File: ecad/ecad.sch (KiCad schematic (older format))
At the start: 27 parts, among them J1 Conn_01x03_Female, J10 Conn_01x05_Female, J4 Conn_01x03_Female, J5 Conn_01x03_Female, J6 Conn_01x03_Female, J7 Conn_01x05_Female, J8 Conn_01x05_Female, J9 Conn_01x05_Female, U1 DHT11, U2 ABX00012

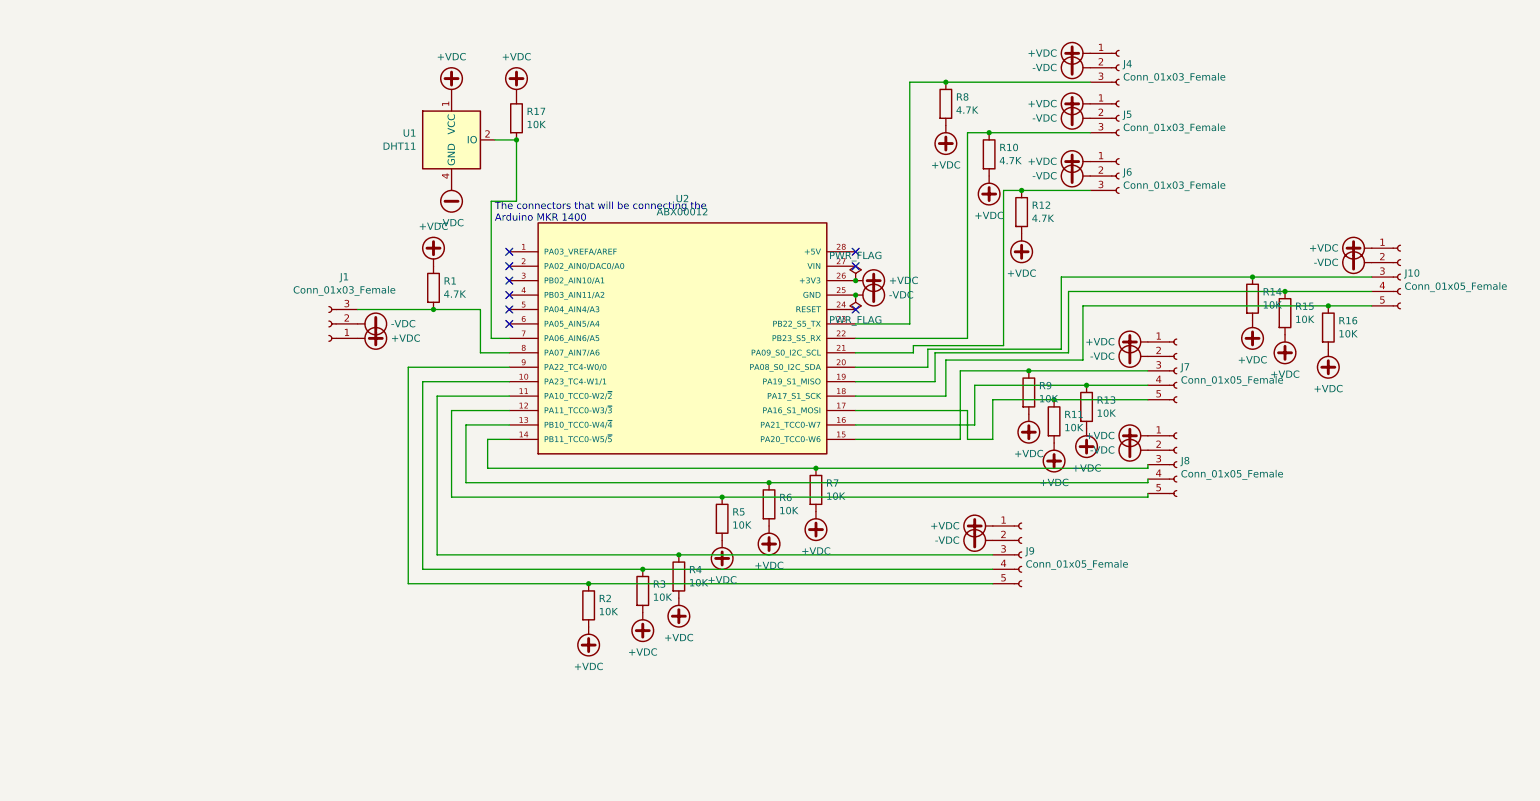
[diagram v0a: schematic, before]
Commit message: add more comments to the schematic
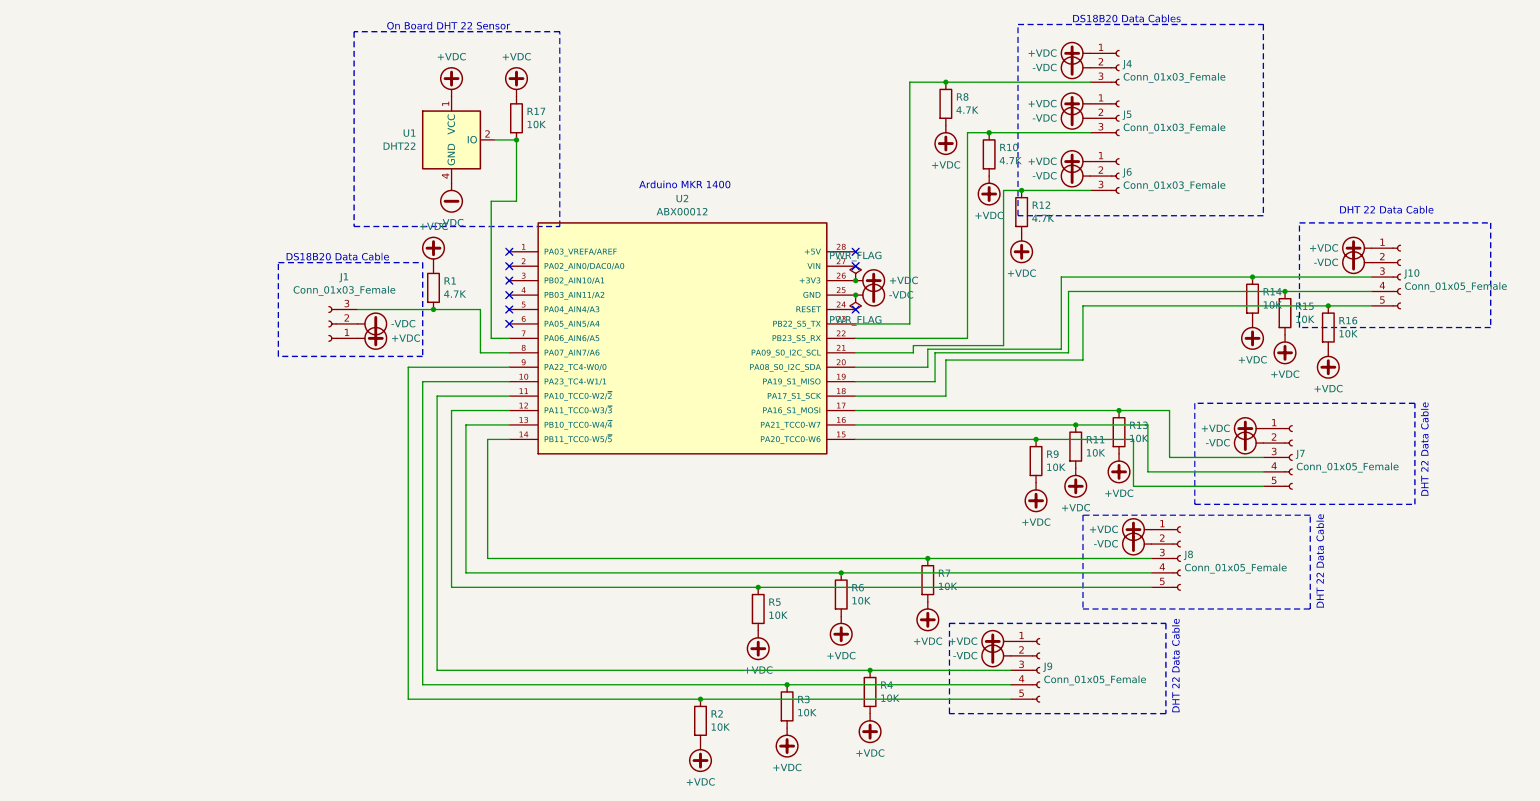
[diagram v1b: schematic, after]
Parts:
- U1: value DHT11 -> DHT22
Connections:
- net at R9.1, U2.15 (PA20_TCC0-W6): now also J7.5 (Pin_5); no longer J7.3 (Pin_3)
- net at J7.4 (Pin_4), U2.16 (PA21_TCC0-W7): now also R11.1; no longer R13.1
- new net: J7.3 (Pin_3), R13.1, U2.17 (PA16_S1_MOSI)
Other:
- note added: "Arduino MKR 1400"
- note added: "DHT 22 Data Cable"
- note added: "DS18B20 Data Cable"
- note added: "DS18B20 Data Cables"
- note added: "On Board DHT 22 Sensor"
- note removed: "The connectors that will be connecting the \nArduino MKR 1400"
- moved on the sheet: J7, J8, J9, R11, R13, R2, R3, R4, R5, R6, R7, R9

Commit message: make pcb smaller and only one wire for each cable
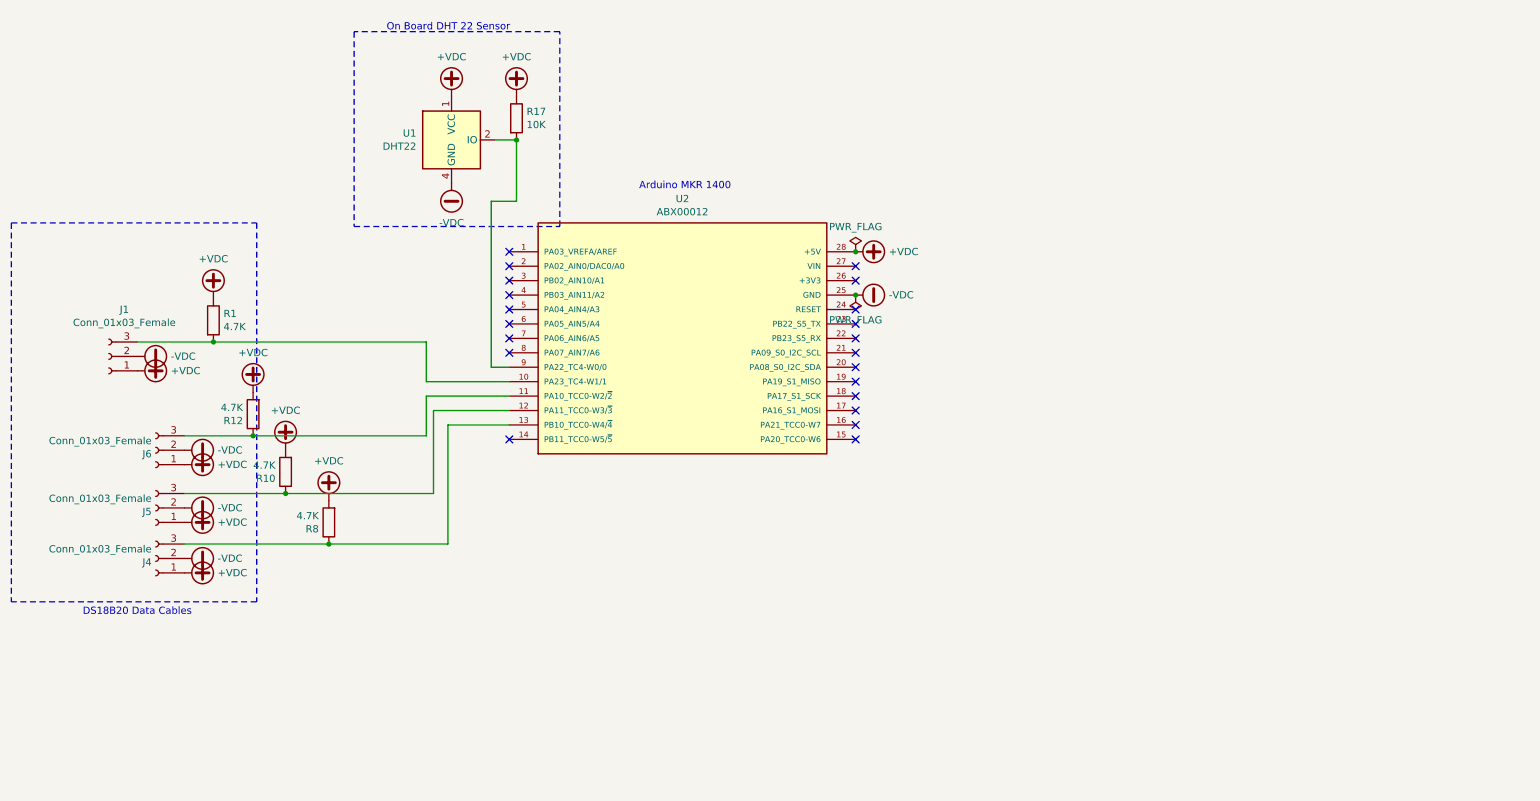
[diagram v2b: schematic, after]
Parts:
- removed J10, J7, J8, J9: Conn_01x05_Female, digikey-footprints:Wago_734-135_1x05_P5.0mm_Vertical, symbol Connector:Conn_01x05_Female
- removed R11, R13, R14, R15, R16, R2, R3, R4, R5, R6, R7, R9: 10K, Resistor_THT:R_Axial_DIN0207_L6.3mm_D2.5mm_P7.62mm_Horizontal, symbol Device:R
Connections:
- net +VDC: now also U2.28 (+5V); no longer U2.26 (+3V3)
- net at U2.13 (PB10_TCC0-W4/~4): now also J4.3 (Pin_3), R8.1
- net at U2.12 (PA11_TCC0-W3/~3): now also J5.3 (Pin_3), R10.1
- net at U2.11 (PA10_TCC0-W2/~2): now also J6.3 (Pin_3), R12.1
- net at U2.10 (PA23_TC4-W1/1): now also J1.3 (Pin_3), R1.2
- net at U2.9 (PA22_TC4-W0/0): now also R17.2, U1.2 (IO)
- now unconnected: U2.21 (PA09_S0_I2C_SCL), U2.22 (PB23_S5_RX), U2.23 (PB22_S5_TX), U2.7 (PA06_AIN6/A5), U2.8 (PA07_AIN7/A6)
- no-connect marks 9 -> 21
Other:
- note removed: "DHT 22 Data Cable"
- note removed: "DS18B20 Data Cable"
- moved on the sheet: J1, J4, J5, J6, R1, R10, R12, R8

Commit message: updated pcb to use 3.3V instead of 5V
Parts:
- J1, J4, J5, J6: symbol Connector:Conn_01x03_Female -> ecad-rescue:Conn_01x03_Female-Connector
- R1, R10, R12, R17, R8: symbol Device:R -> ecad-rescue:R-Device
- U1: symbol Sensor:DHT11 -> ecad-rescue:DHT11-Sensor
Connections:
- net +VDC: now also U2.26 (+3V3); no longer U2.28 (+5V)
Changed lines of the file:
@@
 Arduino MKR 1400
 $Comp
-L power:+VDC #PWR0102
+L ecad-rescue:+VDC-power #PWR0102
 U 1 1 60A8C83E
-P 6700 2650
-F 0 "#PWR0102" H 6700 2550 50  0001 C CNN
-F 1 "+VDC" V 6700 2880 50  0000 L CNN
-F 2 "" H 6700 2650 50  0001 C CNN
-F 3 "" H 6700 2650 50  0001 C CNN
-	1    6700 2650
-	0    1    1    0
-$EndComp
-$Comp
-L power:-VDC #PWR0110
+P 6700 2850
+F 0 "#PWR0102" H 6700 2750 50  0001 C CNN
+F 1 "+VDC" V 6700 3080 50  0000 L CNN
+F 2 "" H 6700 2850 50  0001 C CNN
+F 3 "" H 6700 2850 50  0001 C CNN
+	1    6700 2850
+	0    1    1    0
+$EndComp
+$Comp
+L ecad-rescue:-VDC-power #PWR0110
 U 1 1 60A90684
 P 6700 2950
@@
 $EndComp
 $Comp
-L Connector:Conn_01x03_Female J6
+L ecad-rescue:Conn_01x03_Female-Connector J6
 U 1 1 60A99987
 P 1850 4025
@@
 $EndComp
 $Comp
-L Connector:Conn_01x03_Female J5
+L ecad-rescue:Conn_01x03_Female-Connector J5
 U 1 1 60A9AE52
 P 1850 4425
@@
 $EndComp
 $Comp
-L Connector:Conn_01x03_Female J4
+L ecad-rescue:Conn_01x03_Female-Connector J4
 U 1 1 60A9B632
 P 1850 4775
@@
 $EndComp
 $Comp
-L Connector:Conn_01x03_Female J1
+L ecad-rescue:Conn_01x03_Female-Connector J1
 U 1 1 60A9BC86
 P 1525 3375
@@
 $EndComp
 $Comp
-L power:+VDC #PWR0111
+L ecad-rescue:+VDC-power #PWR0111
 U 1 1 60A9C88A
 P 2050 4875
@@
 $EndComp
 $Comp
-L power:+VDC #PWR0112
+L ecad-rescue:+VDC-power #PWR0112
 U 1 1 60A9CDFE
 P 2050 4525
@@
 $EndComp
 $Comp
-L power:+VDC #PWR0113
+L ecad-rescue:+VDC-power #PWR0113
 U 1 1 60A9D77B
 P 2050 4125
@@
 $EndComp
 $Comp
-L power:+VDC #PWR0114
+L ecad-rescue:+VDC-power #PWR0114
 U 1 1 60A9DE4F
 P 1725 3475
@@
 $EndComp
 $Comp
-L power:-VDC #PWR0115
+L ecad-rescue:-VDC-power #PWR0115
 U 1 1 60A9EA52
 P 2050 4025
@@
 $EndComp
 $Comp
-L power:-VDC #PWR0116
+L ecad-rescue:-VDC-power #PWR0116
 U 1 1 60A9F122
 P 2050 4425
@@
 $EndComp
 $Comp
-L power:-VDC #PWR0117
+L ecad-rescue:-VDC-power #PWR0117
 U 1 1 60A9F7F5
 P 2050 4775
@@
 $EndComp
 $Comp
-L power:-VDC #PWR0118
+L ecad-rescue:-VDC-power #PWR0118
 U 1 1 60A9FE62
 P 1725 3375
@@
 	2050 4675 3050 4675
 $Comp
-L Device:R R12
+L ecad-rescue:R-Device R12
 U 1 1 60ACB0F8
 P 2525 3775
@@
 $EndComp
 $Comp
-L Device:R R10
+L ecad-rescue:R-Device R10
 U 1 1 60ACC577
 P 2750 4175
@@
 $EndComp
 $Comp
-L Device:R R8
+L ecad-rescue:R-Device R8
 U 1 1 60ACCC23
 P 3050 4525
@@
 $EndComp
 $Comp
-L Device:R R1
+L ecad-rescue:R-Device R1
 U 1 1 60ACE3A2
 P 2250 3125
@@
 $EndComp
 $Comp
-L power:+VDC #PWR0119
+L ecad-rescue:+VDC-power #PWR0119
 U 1 1 60ACF716
 P 2250 2975
@@
 $EndComp
 $Comp
-L power:+VDC #PWR0120
+L ecad-rescue:+VDC-power #PWR0120
 U 1 1 60ACFFF3
 P 3050 4375
@@
 $EndComp
 $Comp
-L power:+VDC #PWR0121
+L ecad-rescue:+VDC-power #PWR0121
 U 1 1 60AD34D1
 P 2750 4025
@@
 $EndComp
 $Comp
-L power:+VDC #PWR0122
+L ecad-rescue:+VDC-power #PWR0122
 U 1 1 60AD3D4F
 P 2525 3625
@@
 NoConn ~ 4300 3050
 $Comp
-L power:PWR_FLAG #FLG0102
+L ecad-rescue:PWR_FLAG-power #FLG0102
 U 1 1 60B51A82
-P 6700 2650
-F 0 "#FLG0102" H 6700 2725 50  0001 C CNN
-F 1 "PWR_FLAG" H 6700 2823 50  0000 C CNN
-F 2 "" H 6700 2650 50  0001 C CNN
-F 3 "~" H 6700 2650 50  0001 C CNN
-	1    6700 2650
-	1    0    0    -1
-$EndComp
-$Comp
-L power:PWR_FLAG #FLG0101
+P 6700 2850
+F 0 "#FLG0102" H 6700 2925 50  0001 C CNN
+F 1 "PWR_FLAG" H 6700 3023 50  0000 C CNN
+F 2 "" H 6700 2850 50  0001 C CNN
+F 3 "~" H 6700 2850 50  0001 C CNN
+	1    6700 2850
+	1    0    0    -1
+$EndComp
+$Comp
+L ecad-rescue:PWR_FLAG-power #FLG0101
 U 1 1 60B580F0
 P 6700 2950
@@
 $EndComp
 $Comp
-L Sensor:DHT11 U1
+L ecad-rescue:DHT11-Sensor U1
 U 1 1 60B5D90B
 P 3900 1875
@@
 $EndComp
 $Comp
-L power:+VDC #PWR01
+L ecad-rescue:+VDC-power #PWR01
 U 1 1 60B62AE8
 P 3900 1575
@@
 $EndComp
 $Comp
-L power:-VDC #PWR02
+L ecad-rescue:-VDC-power #PWR02
 U 1 1 60B6473C
 P 3900 2175
@@
 	4350 2300 4175 2300
 $Comp
-L Device:R R17
+L ecad-rescue:R-Device R17
 U 1 1 60B733B1
 P 4350 1725
@@
 Connection ~ 4350 1875
 $Comp
-L power:+VDC #PWR03
+L ecad-rescue:+VDC-power #PWR03
 U 1 1 60B74477
 P 4350 1575
@@
 Text Notes 3450 1125 0    50   ~ 0
 On Board DHT 22 Sensor
-Connection ~ 6700 2650
-NoConn ~ 6700 2850
 Wire Wire Line
 	4175 3450 4300 3450
@@
 NoConn ~ 6700 3850
 NoConn ~ 6700 3950
+Connection ~ 6700 2850
+NoConn ~ 6700 2650
 $EndSCHEMATC
